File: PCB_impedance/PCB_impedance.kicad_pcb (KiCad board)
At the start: 2 copper layers, 43 parts, among them J1 Screw_Terminal_01x04, J2 Conn_02x20_Odd_Even, J3 Screw_Terminal_01x04, J4 Screw_Terminal_01x04, J5 Screw_Terminal_01x04, U1 CD74HC4067M, U2 CD74HC4067M, U3 CD74HC4067M, U4 CD74HC4067M, U6 AD5941, U7 MCP1727-3302xMF

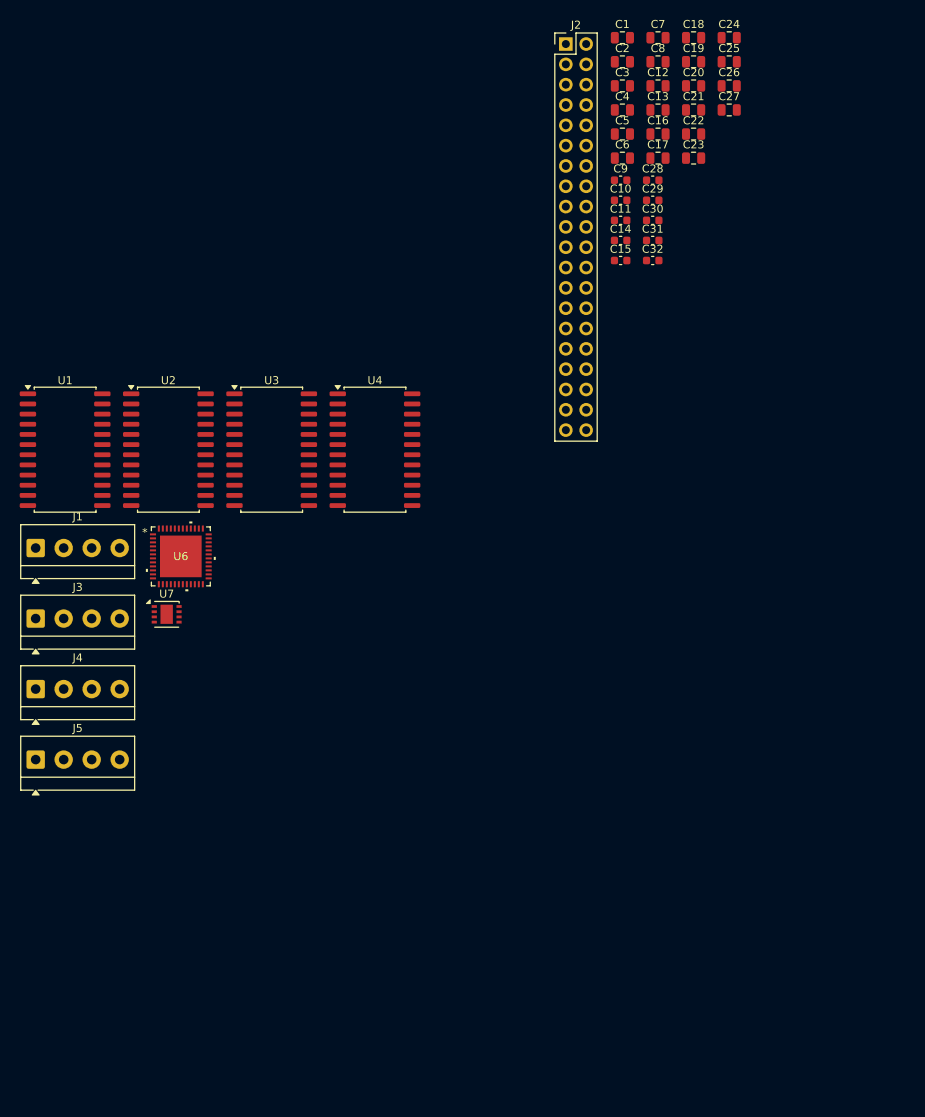
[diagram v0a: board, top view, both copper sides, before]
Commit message: Correction to the PCB schematic for measuring impedance (replacement of the multiplexer and add new connector for electrodes)
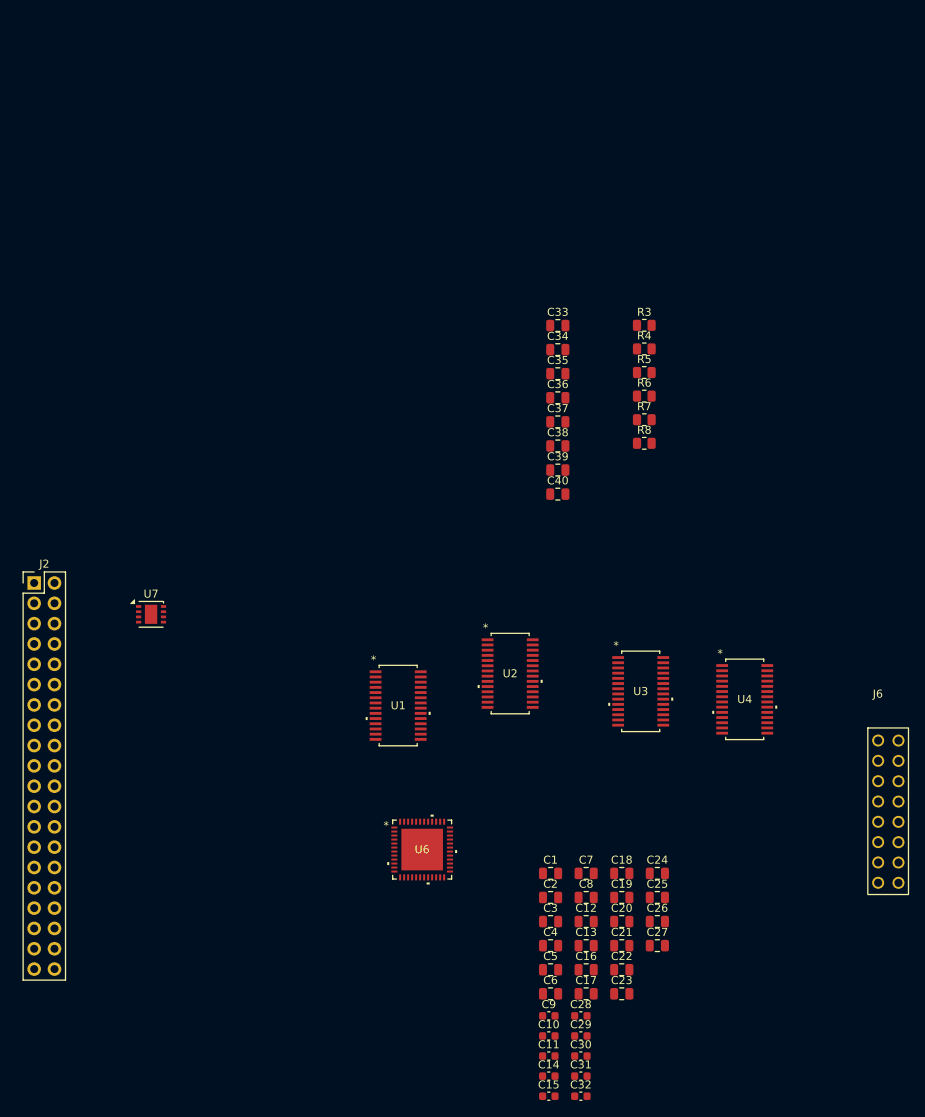
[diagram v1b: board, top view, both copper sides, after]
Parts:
- removed J1, J3, J4, J5: Screw_Terminal_01x04, AAA_MAZZA_project:TerminalBlock_MetzConnect_Type059_RT06304HBWC_1x04_P3.50mm_Horizontal
- added C33: 10u, Capacitor_SMD:C_0805_2012Metric, F.Cu at (122.0, 47.0)
- added C34: 100n, Capacitor_SMD:C_0805_2012Metric, F.Cu at (122.0, 50.0)
- added C35: 100n, Capacitor_SMD:C_0805_2012Metric, F.Cu at (122.0, 53.0)
- added C36: 10u, Capacitor_SMD:C_0805_2012Metric, F.Cu at (122.0, 56.0)
- added C37: 100n, Capacitor_SMD:C_0805_2012Metric, F.Cu at (122.0, 59.0)
- added C38: 10u, Capacitor_SMD:C_0805_2012Metric, F.Cu at (122.0, 62.0)
- added C39: 100n, Capacitor_SMD:C_0805_2012Metric, F.Cu at (122.0, 65.1)
- added C40: 10u, Capacitor_SMD:C_0805_2012Metric, F.Cu at (122.0, 68.1)
- added J6: Conn_01x16_Socket, lib_mesure_impedance:conn_1x16_PPPC082LFBN-RC, F.Cu at (160.7, 97.3)
- added R3: 10, Resistor_SMD:R_0805_2012Metric, F.Cu at (132.8, 47.0)
- added R4: 10k, Resistor_SMD:R_0805_2012Metric, F.Cu at (132.8, 49.9)
- added R5: 1k, Resistor_SMD:R_0805_2012Metric, F.Cu at (132.8, 52.9)
- added R6: 1k, Resistor_SMD:R_0805_2012Metric, F.Cu at (132.8, 55.8)
- added R7: 0R, Resistor_SMD:R_0805_2012Metric, F.Cu at (132.8, 58.8)
- added R8: 0R, Resistor_SMD:R_0805_2012Metric, F.Cu at (132.8, 61.7)
- U1, U2, U3, U4: value CD74HC4067M -> ADG706BRUZ-REEL; footprint Package_SO:SOIC-24W_7.5x15.4mm_P1.27mm -> lib_mesure_impedance:ADG706BRUZ
- U6: footprint AAA_MAZZA_project:AD5941_footprint -> lib_mesure_impedance:AD5941_footprint
- moved C1 104.8 mm to (121.0, 115.5)
- moved C10 104.8 mm to (120.8, 135.8)
- moved C11 104.8 mm to (120.8, 138.3)
- moved C12 104.8 mm to (125.5, 121.5)
- moved C13 104.8 mm to (125.5, 124.5)
- moved C15 104.8 mm to (120.8, 143.3)
- moved C17 104.8 mm to (125.5, 130.5)
- moved C18 104.8 mm to (129.9, 115.5)
- moved C20 104.8 mm to (129.9, 121.5)
- moved C21 104.8 mm to (129.9, 124.5)
- moved C23 104.8 mm to (129.9, 130.5)
- moved C24 104.8 mm to (134.4, 115.5)
- moved C26 104.8 mm to (134.4, 121.5)
- moved C27 104.8 mm to (134.4, 124.5)
- moved C29 104.8 mm to (124.8, 135.8)
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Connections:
- C10 pad 1: Net-(U6-AVDD_REG) -> Net-(U6-DVDD_REG_1V8)
- J2 pad 11: /MUX_En2 -> /MUX_EN2
- J2 pad 13: /MUX_En3 -> /MUX_EN3
- J2 pad 15: unconnected-(J2-Pin_15-Pad15) -> /MUX_S0
- J2 pad 16: unconnected-(J2-Pin_16-Pad16) -> /MUX_S8
- J2 pad 17: unconnected-(J2-Pin_17-Pad17) -> /MUX_S1
- J2 pad 18: unconnected-(J2-Pin_18-Pad18) -> /MUX_S9
- J2 pad 22: unconnected-(J2-Pin_22-Pad22) -> /MUX_S10
- J2 pad 26: unconnected-(J2-Pin_26-Pad26) -> /MUX_S11
- J2 pad 27: /MUX_S0 -> /MUX_S2
- J2 pad 28: unconnected-(J2-Pin_28-Pad28) -> /MUX_S12
- J2 pad 29: /MUX_S1 -> /MUX_S3
- J2 pad 31: /MUX_S2 -> /MUX_S4
- J2 pad 32: unconnected-(J2-Pin_32-Pad32) -> /MUX_S13
- J2 pad 33: /MUX_S3 -> /MUX_S5
- J2 pad 35: unconnected-(J2-Pin_35-Pad35) -> /MUX_S6
- J2 pad 36: unconnected-(J2-Pin_36-Pad36) -> /MUX_S14
- J2 pad 37: unconnected-(J2-Pin_37-Pad37) -> /MUX_S7
- J2 pad 38: unconnected-(J2-Pin_38-Pad38) -> /MUX_S15
- J2 pad 5: /MUX_En0 -> /MUX_EN0
- J2 pad 7: /MUX_En1 -> /MUX_EN1
- U1 pad 1: /F- -> +3V3
- U1 pad 10: /MUX_S0 -> /E10
- U1 pad 11: /MUX_S1 -> /E9
- U1 pad 13: /MUX_S3 -> unconnected-(U1-NC-Pad13)_1
- U1 pad 14: /MUX_S2 -> /MUX_S15
- U1 pad 15: /MUX_En1 -> /MUX_S14
- U1 pad 16: /E15 -> /MUX_S13
- U1 pad 17: /E14 -> /MUX_S12
- U1 pad 18: /E13 -> /MUX_EN3
- U1 pad 19: /E12 -> /E1
- U1 pad 2: /E7 -> unconnected-(U1-NC-Pad13)
- U1 pad 20: /E11 -> /E2
- U1 pad 21: /E10 -> /E3
- U1 pad 22: /E9 -> /E4
- U1 pad 23: /E8 -> /E5
- U1 pad 24: +3V3 -> /E6
- U1 pad 3: /E6 -> unconnected-(U1-NC-Pad13)_2
- U1 pad 4: /E5 -> /E16
- U1 pad 5: /E4 -> /E15
- U1 pad 6: /E3 -> /E14
- U1 pad 7: /E2 -> /E13
- U1 pad 8: /E1 -> /E12
- U1 pad 9: /E0 -> /E11
- U2 pad 1: /S+ -> +3V3
- U2 pad 10: /MUX_S0 -> /E10
- U2 pad 11: /MUX_S1 -> /E9
- U2 pad 13: /MUX_S3 -> unconnected-(U2-NC-Pad13)_2
- U2 pad 14: /MUX_S2 -> /MUX_S11
- U2 pad 15: /MUX_En2 -> /MUX_S10
- U2 pad 16: /E15 -> /MUX_S9
- U2 pad 17: /E14 -> /MUX_S8
- U2 pad 18: /E13 -> /MUX_EN2
- U2 pad 19: /E12 -> /E1
- U2 pad 2: /E7 -> unconnected-(U2-NC-Pad13)
- U2 pad 20: /E11 -> /E2
- U2 pad 21: /E10 -> /E3
- U2 pad 22: /E9 -> /E4
- U2 pad 23: /E8 -> /E5
- U2 pad 24: +3V3 -> /E6
- U2 pad 3: /E6 -> unconnected-(U2-NC-Pad13)_1
- U2 pad 4: /E5 -> /E16
- U2 pad 5: /E4 -> /E15
- U2 pad 6: /E3 -> /E14
- U2 pad 7: /E2 -> /E13
- U2 pad 8: /E1 -> /E12
- U2 pad 9: /E0 -> /E11
- U3 pad 1: /F+ -> +3V3
- U3 pad 10: /MUX_S0 -> /E10
- U3 pad 11: /MUX_S1 -> /E9
- U3 pad 13: /MUX_S3 -> unconnected-(U3-NC-Pad13)
- U3 pad 14: /MUX_S2 -> /MUX_S7
- U3 pad 15: /MUX_En0 -> /MUX_S6
- U3 pad 16: /E15 -> /MUX_S5
- U3 pad 17: /E14 -> /MUX_S4
- U3 pad 18: /E13 -> /MUX_EN1
- U3 pad 19: /E12 -> /E1
- U3 pad 2: /E7 -> unconnected-(U3-NC-Pad13)_1
- U3 pad 20: /E11 -> /E2
- U3 pad 21: /E10 -> /E3
- U3 pad 22: /E9 -> /E4
- U3 pad 23: /E8 -> /E5
- U3 pad 24: +3V3 -> /E6
- U3 pad 3: /E6 -> unconnected-(U3-NC-Pad13)_2
- U3 pad 4: /E5 -> /E16
- U3 pad 5: /E4 -> /E15
- U3 pad 6: /E3 -> /E14
- U3 pad 7: /E2 -> /E13
- U3 pad 8: /E1 -> /E12
- U3 pad 9: /E0 -> /E11
- U4 pad 1: /S- -> +3V3
- U4 pad 10: /MUX_S0 -> /E10
- U4 pad 11: /MUX_S1 -> /E9
- U4 pad 13: /MUX_S3 -> unconnected-(U4-NC-Pad13)_1
- U4 pad 14: /MUX_S2 -> /MUX_S3
- U4 pad 15: /MUX_En3 -> /MUX_S2
- U4 pad 16: /E15 -> /MUX_S1
- U4 pad 17: /E14 -> /MUX_S0
- U4 pad 18: /E13 -> /MUX_EN0
- U4 pad 19: /E12 -> /E1
- U4 pad 2: /E7 -> unconnected-(U4-NC-Pad13)_2
- U4 pad 20: /E11 -> /E2
- U4 pad 21: /E10 -> /E3
- U4 pad 22: /E9 -> /E4
- U4 pad 23: /E8 -> /E5
- U4 pad 24: +3V3 -> /E6
- U4 pad 3: /E6 -> unconnected-(U4-NC-Pad13)
- U4 pad 4: /E5 -> /E16
- U4 pad 5: /E4 -> /E15
- U4 pad 6: /E3 -> /E14
- U4 pad 7: /E2 -> /E13
- U4 pad 8: /E1 -> /E12
- U4 pad 9: /E0 -> /E11
- U6 pad 14: Net-(U6-AVDD_REG) -> Net-(U6-DVDD_REG_1V8)

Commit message: Multiplexer routing complete
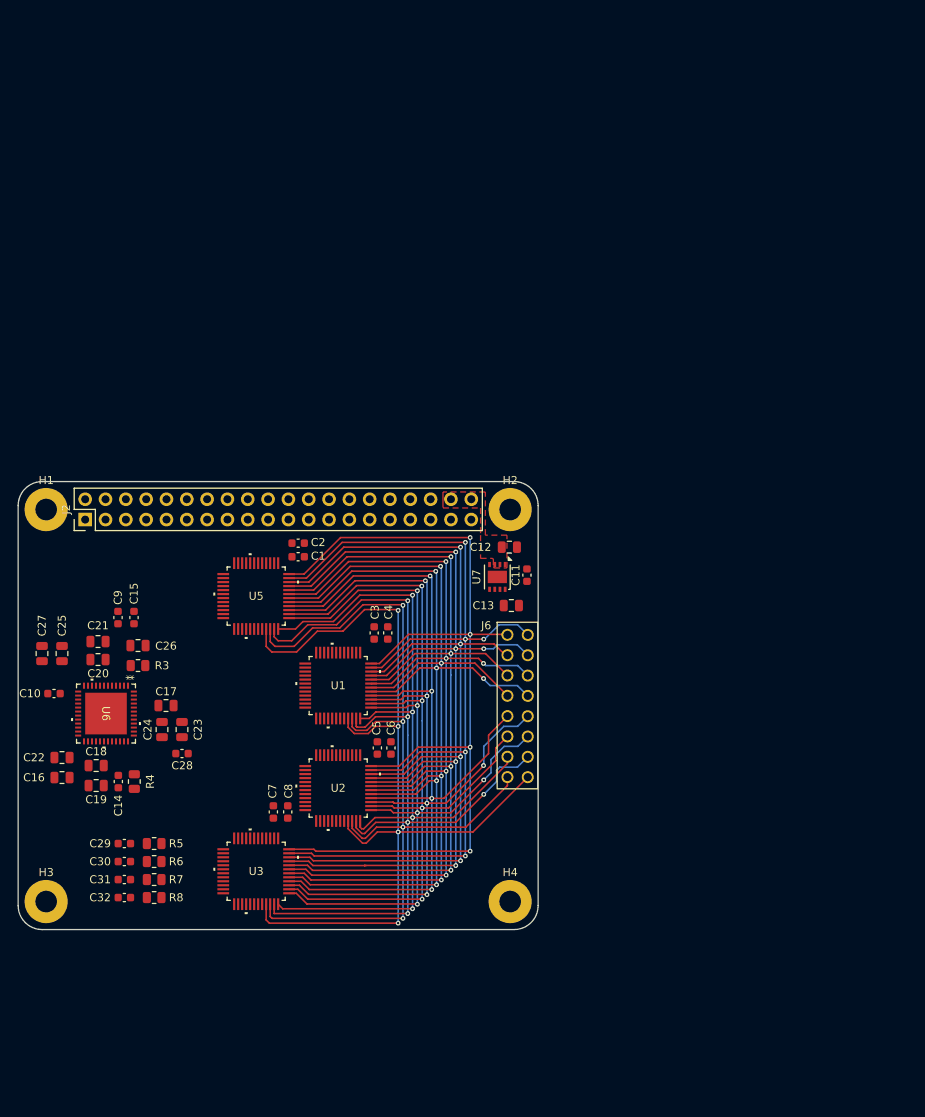
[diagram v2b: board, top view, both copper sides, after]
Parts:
- removed C33, C36, C38, C40: 10u, Capacitor_SMD:C_0805_2012Metric
- removed C34, C35, C37, C39: 100n, Capacitor_SMD:C_0805_2012Metric
- removed U4: ADG706BRUZ-REEL, lib_mesure_impedance:ADG706BRUZ
- added H1: MountingHole, MountingHole:MountingHole_2.7mm_Pad, F.Cu at (58.0, 70.0)
- added H2: MountingHole, MountingHole:MountingHole_2.7mm_Pad, F.Cu at (116.0, 70.0)
- added H3: MountingHole, MountingHole:MountingHole_2.7mm_Pad, F.Cu at (58.0, 119.0)
- added H4: MountingHole, MountingHole:MountingHole_2.7mm_Pad, F.Cu at (116.0, 119.0)
- added U5: ADG726BSUZ, lib_mesure_impedance:ADG726SBUZ, F.Cu at (84.2, 80.8)
- C1, C3, C5, C7: value 10u -> 100n; footprint Capacitor_SMD:C_0805_2012Metric -> Capacitor_SMD:C_0603_1608Metric
- C2, C4, C6, C8: value 100n -> 10u; footprint Capacitor_SMD:C_0805_2012Metric -> Capacitor_SMD:C_0603_1608Metric
- J2: footprint Connector_PinHeader_2.54mm:PinHeader_2x20_P2.54mm_Vertical -> lib_mesure_impedance:PinHeader_2x20_P2.54mm_Vertical
- U1, U2, U3: value ADG706BRUZ-REEL -> ADG726BSUZ; footprint lib_mesure_impedance:ADG706BRUZ -> lib_mesure_impedance:ADG726SBUZ
- moved C27 85.1 mm to (57.5, 88.0), turned to 90 degrees
- moved R5 85.0 mm to (71.5, 111.8), turned to 180 degrees
- moved R6 84.5 mm to (71.5, 114.0), turned to 180 degrees
- moved R7 84.0 mm to (71.5, 116.2), turned to 180 degrees
- moved R4 83.6 mm to (69.0, 104.0), turned to 90 degrees
- moved R8 83.5 mm to (71.5, 118.5), turned to 180 degrees
- moved C25 80.4 mm to (60.0, 88.0), turned to 90 degrees
- moved C15 79.2 mm to (69.0, 83.5), turned to 90 degrees
- moved R3 76.3 mm to (69.5, 89.5), turned to 180 degrees
- moved C21 75.7 mm to (64.5, 86.5), turned to 180 degrees
- moved C10 75.2 mm to (59.0, 93.0), turned to 180 degrees
- moved C22 74.8 mm to (60.0, 101.0), turned to 180 degrees
- moved C26 73.5 mm to (69.5, 87.0), turned to 180 degrees
- moved C9 73.3 mm to (67.0, 83.5), turned to 90 degrees
- moved C20 73.2 mm to (64.5, 88.8), turned to 180 degrees
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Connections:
- net Net-(C29-Pad1) renamed /F+_node
- net Net-(C30-Pad2) renamed /F-_node
- net Net-(C31-Pad2) renamed /S+_node
- net Net-(C32-Pad2) renamed /S-_node
- J2 pad 11: /MUX_EN2 -> unconnected-(J2-Pin_11-Pad11)
- J2 pad 13: /MUX_EN3 -> /MUX_EN0
- J2 pad 15: /MUX_S0 -> /MUX_EN1
- J2 pad 16: /MUX_S8 -> unconnected-(J2-Pin_16-Pad16)
- J2 pad 17: /MUX_S1 -> unconnected-(J2-Pin_17-Pad17)
- J2 pad 18: /MUX_S9 -> /MUX_WR0
- J2 pad 22: /MUX_S10 -> /MUX_WR1
- J2 pad 26: /MUX_S11 -> /MUX_WR2
- J2 pad 27: /MUX_S2 -> /MUX_EN2
- J2 pad 28: /MUX_S12 -> /MUX_WR3
- J2 pad 29: /MUX_S3 -> /MUX_EN3
- J2 pad 31: /MUX_S4 -> /MUX_A0
- J2 pad 32: /MUX_S13 -> /MUX_CSA0
- J2 pad 33: /MUX_S5 -> /MUX_A1
- J2 pad 35: /MUX_S6 -> /MUX_A2
- J2 pad 36: /MUX_S14 -> /MUX_CSA1
- J2 pad 37: /MUX_S7 -> /MUX_A3
- J2 pad 38: /MUX_S15 -> /MUX_CSA2
- J2 pad 40: unconnected-(J2-Pin_40-Pad40) -> /MUX_CSA3
- J2 pad 5: /MUX_EN0 -> unconnected-(J2-Pin_5-Pad5)
- J2 pad 7: /MUX_EN1 -> unconnected-(J2-Pin_7-Pad7)
- U1 pad 1: +3V3 -> /E12
- U1 pad 10: /E10 -> /E3
- U1 pad 11: /E9 -> /E2
- U1 pad 12: GND -> /E1
- U1 pad 13: unconnected-(U1-NC-Pad13)_1 -> +3V3
- U1 pad 14: /MUX_S15 -> +3V3
- U1 pad 15: /MUX_S14 -> /MUX_A0
- U1 pad 16: /MUX_S13 -> /MUX_A1
- U1 pad 17: /MUX_S12 -> /MUX_A2
- U1 pad 18: /MUX_EN3 -> /MUX_A3
- U1 pad 19: /E1 -> /MUX_CSA1
- U1 pad 2: unconnected-(U1-NC-Pad13) -> /E11
- U1 pad 20: /E2 -> +3V3
- U1 pad 21: /E3 -> /MUX_WR1
- U1 pad 22: /E4 -> /MUX_EN1
- U1 pad 23: /E5 -> GND
- U1 pad 24: /E6 -> GND
- U1 pad 25: /E7 -> unconnected-(U1-S1B-Pad25)
- U1 pad 26: /E8 -> unconnected-(U1-S2B-Pad26)
- U1 pad 27: GND -> unconnected-(U1-S3B-Pad27)
- U1 pad 28: /S- -> unconnected-(U1-S4B-Pad28)
- U1 pad 3: unconnected-(U1-NC-Pad13)_2 -> /E10
- U1 pad 4: /E16 -> /E9
- U1 pad 5: /E15 -> /E8
- U1 pad 6: /E14 -> /E7
- U1 pad 7: /E13 -> /E6
- U1 pad 8: /E12 -> /E5
- U1 pad 9: /E11 -> /E4
- U2 pad 1: +3V3 -> /E12
- U2 pad 10: /E10 -> /E3
- U2 pad 11: /E9 -> /E2
- U2 pad 12: GND -> /E1
- U2 pad 13: unconnected-(U2-NC-Pad13)_2 -> +3V3
- U2 pad 14: /MUX_S11 -> +3V3
- U2 pad 15: /MUX_S10 -> /MUX_A0
- U2 pad 16: /MUX_S9 -> /MUX_A1
- U2 pad 17: /MUX_S8 -> /MUX_A2
- U2 pad 18: /MUX_EN2 -> /MUX_A3
- U2 pad 19: /E1 -> /MUX_CSA2
- U2 pad 2: unconnected-(U2-NC-Pad13) -> /E11
- U2 pad 20: /E2 -> +3V3
- U2 pad 21: /E3 -> /MUX_WR2
- U2 pad 22: /E4 -> /MUX_EN2
- U2 pad 23: /E5 -> GND
- U2 pad 24: /E6 -> GND
- U2 pad 25: /E7 -> unconnected-(U2-S1B-Pad25)
- U2 pad 26: /E8 -> unconnected-(U2-S2B-Pad26)
- U2 pad 27: GND -> unconnected-(U2-S3B-Pad27)
- U2 pad 28: /S+ -> unconnected-(U2-S4B-Pad28)
- U2 pad 3: unconnected-(U2-NC-Pad13)_1 -> /E10
- U2 pad 4: /E16 -> /E9
- U2 pad 5: /E15 -> /E8
- U2 pad 6: /E14 -> /E7
- U2 pad 7: /E13 -> /E6
- U2 pad 8: /E12 -> /E5
- U2 pad 9: /E11 -> /E4
- U3 pad 1: +3V3 -> /E12
- U3 pad 10: /E10 -> /E3
- U3 pad 11: /E9 -> /E2
- U3 pad 12: GND -> /E1
- U3 pad 13: unconnected-(U3-NC-Pad13) -> +3V3
- U3 pad 14: /MUX_S7 -> +3V3
- U3 pad 15: /MUX_S6 -> /MUX_A0
- U3 pad 16: /MUX_S5 -> /MUX_A1
- U3 pad 17: /MUX_S4 -> /MUX_A2
- U3 pad 18: /MUX_EN1 -> /MUX_A3
- U3 pad 19: /E1 -> /MUX_CSA3
- U3 pad 2: unconnected-(U3-NC-Pad13)_1 -> /E11
- U3 pad 20: /E2 -> +3V3
- U3 pad 21: /E3 -> /MUX_WR3
- U3 pad 22: /E4 -> /MUX_EN3
- U3 pad 23: /E5 -> GND
- U3 pad 24: /E6 -> GND
- U3 pad 25: /E7 -> unconnected-(U3-S1B-Pad25)
- U3 pad 26: /E8 -> unconnected-(U3-S2B-Pad26)
- U3 pad 27: GND -> unconnected-(U3-S3B-Pad27)
- U3 pad 28: /F- -> unconnected-(U3-S4B-Pad28)
- U3 pad 3: unconnected-(U3-NC-Pad13)_2 -> /E10
- U3 pad 4: /E16 -> /E9
- U3 pad 5: /E15 -> /E8
- U3 pad 6: /E14 -> /E7
- U3 pad 7: /E13 -> /E6
- U3 pad 8: /E12 -> /E5
- U3 pad 9: /E11 -> /E4
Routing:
- net /E2: track 0.00 -> 120.4 mm, vias 0 -> 5
- net /E1: track 0.00 -> 118.4 mm, vias 0 -> 4
- net /E4: track 0.00 -> 116.2 mm, vias 0 -> 5
- net /E3: track 0.00 -> 115.2 mm, vias 0 -> 4
- net /E16: track 0.00 -> 114.6 mm, vias 0 -> 4
- net /E14: track 0.00 -> 112.5 mm, vias 0 -> 5
- net /E6: track 0.00 -> 112.4 mm, vias 0 -> 5
- net /E5: track 0.00 -> 112.0 mm, vias 0 -> 4
- net /E15: track 0.00 -> 110.6 mm, vias 0 -> 4
- net /E8: track 0.00 -> 109.1 mm, vias 0 -> 5
- net /E7: track 0.00 -> 108.8 mm, vias 0 -> 4
- net /E10: track 0.00 -> 108.3 mm, vias 0 -> 5
- net /E9: track 0.00 -> 107.2 mm, vias 0 -> 4
- net /E13: track 0.00 -> 105.2 mm, vias 0 -> 4
- net /E12: track 0.00 -> 103.8 mm, vias 0 -> 5
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- added copper zone on In2.Cu, net +3V3
- added copper zone on F.Cu, net +5V
- added copper zone on In1.Cu, net GND
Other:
- board outline added: 65 x 56 mm
- copper layers 2 -> 4
